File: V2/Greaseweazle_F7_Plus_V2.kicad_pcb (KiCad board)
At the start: 2 copper layers, 80 x 50 mm, 73 parts, among them J1 Wurth 694106301002, J10 PIN1X2, J11 PIN1X2, J12 IDC Box Header, J2 USB_B, J3 Molex 105017-1001, J4 TE EI 171826-4, J5 PIN1X3, J6 PIN1X2, J7 PIN1X5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

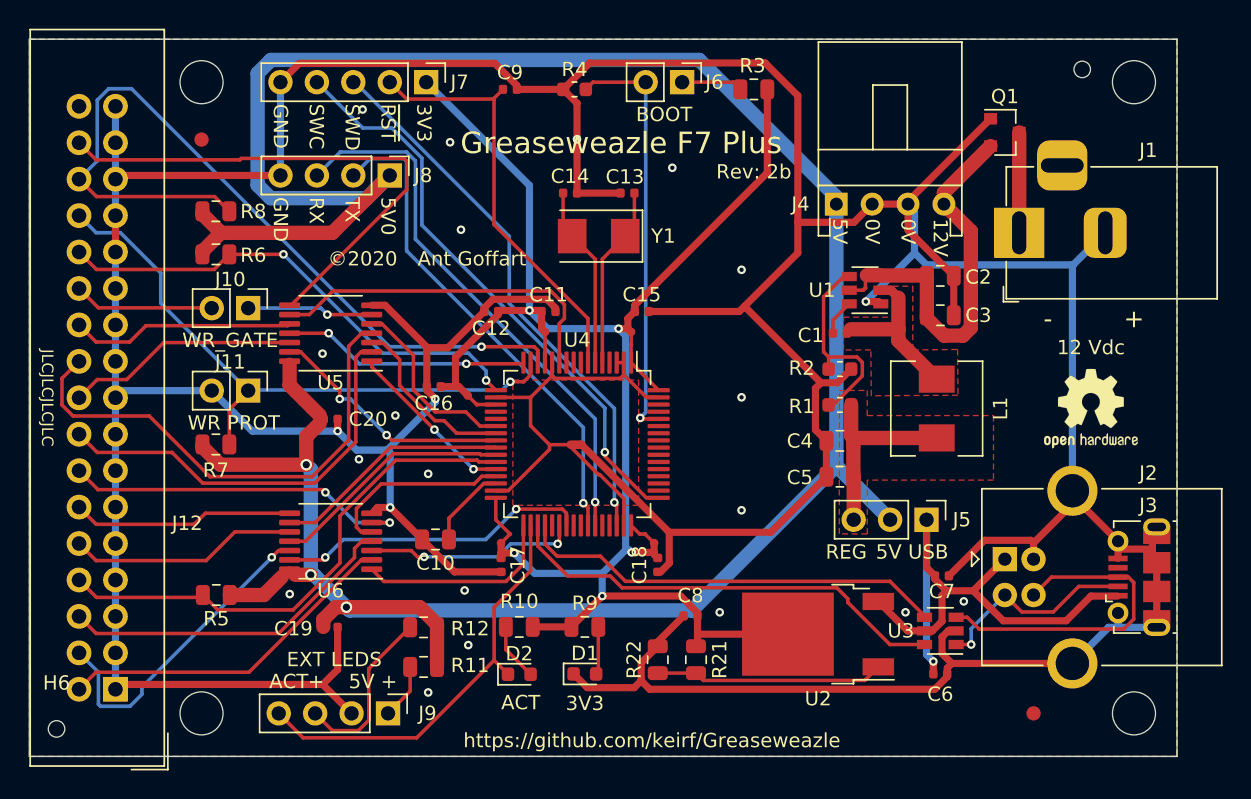
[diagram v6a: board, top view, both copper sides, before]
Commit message: added 3x 10000uF caps to buffer motor start of floppy which can draw up to 1A
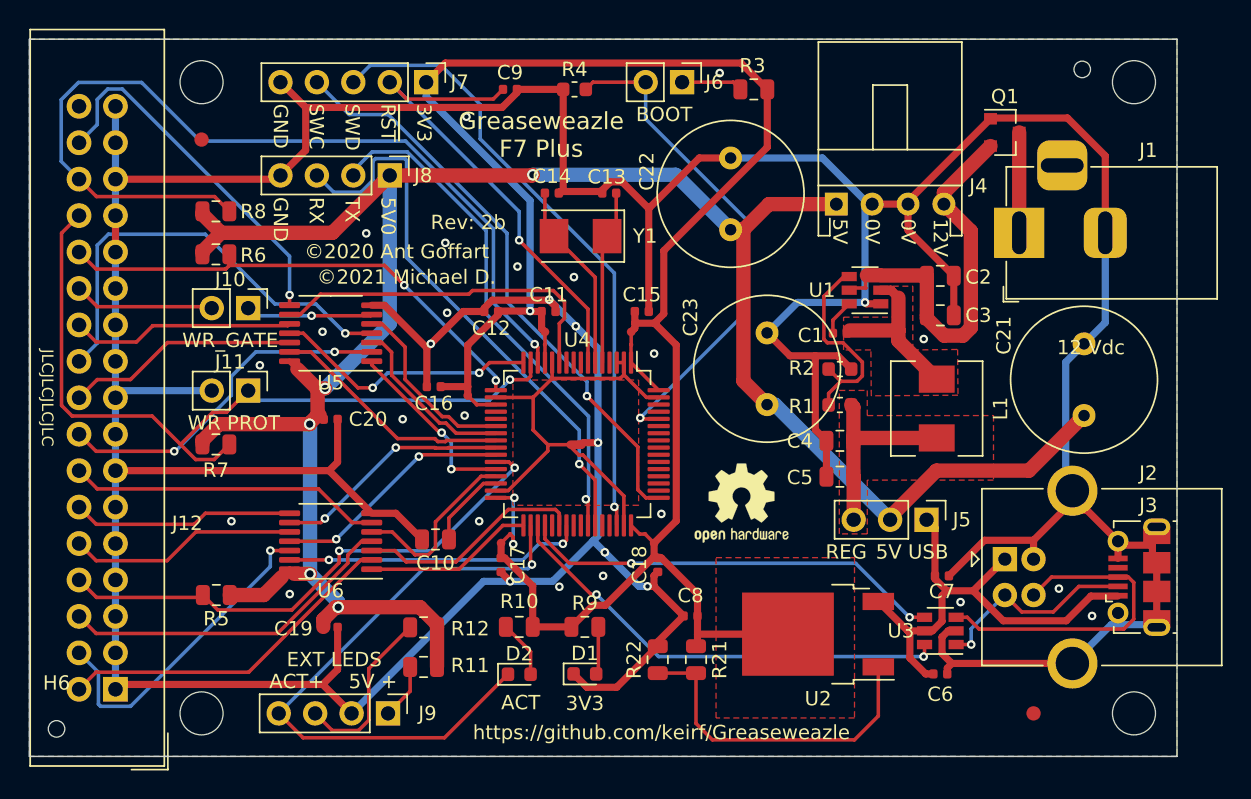
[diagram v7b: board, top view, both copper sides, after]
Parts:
- added C21: 1000uF, Capacitor_THT:C_Radial_D10.0mm_H20.0mm_P5.00mm, F.Cu at (223.5, 126.2)
- added C22: 1000uF, Capacitor_THT:C_Radial_D10.0mm_H20.0mm_P5.00mm, F.Cu at (198.9, 113.3)
- added C23: 1000uF, Capacitor_THT:C_Radial_D10.0mm_H20.0mm_P5.00mm, F.Cu at (201.4, 125.5)
- moved LOGO1 25.2 mm to (199.6, 132.3)
- moved C13 1.27 mm to (190.4, 110.7)
- moved C14 1.27 mm to (186.4, 110.7)
- moved Y1 1.27 mm to (188.4, 113.7)
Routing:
- net +5V: track 189.4 -> 156.2 mm, vias 3 -> 5
- net +3V3: track 113.5 -> 128.7 mm, vias 5 -> 1
- net GND: track 403.6 -> 389.5 mm, vias 23 -> 30
- net /ACT: track 29.8 -> 43.2 mm, vias 0 -> 1
- net /~WR_PROT~: track 43.4 -> 55.3 mm
- net /~SIDE_5V~: track 37.0 -> 25.5 mm, vias 0 -> 1
- net Net-(R21-Pad2): track 16.0 -> 23.5 mm
- net /USB_VBUS: track 41.0 -> 34.0 mm, vias 1 -> 0
- net /~RD_DAT~: track 56.9 -> 62.9 mm
- net /BOOT: track 29.3 -> 35.1 mm
- net /SWDIO: track 38.6 -> 43.7 mm
- net /~M1_5V~: track 29.1 -> 24.5 mm, vias 0 -> 2
- net /~STEP_5V~: track 35.2 -> 30.9 mm, vias 0 -> 1
- net /~RST~: track 29.8 -> 33.9 mm, vias 0 -> 1
- net /~DS0_5V~: track 24.4 -> 21.9 mm, vias 2 -> 0
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- added copper zone on F.Cu, net +3V3
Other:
- board text added: "©2020 Ant Goffart"
- board text added: "©2021 Michael D."
- board text removed: "-"
- board text removed: "Ant Goffart"
- board text removed: "©2020"

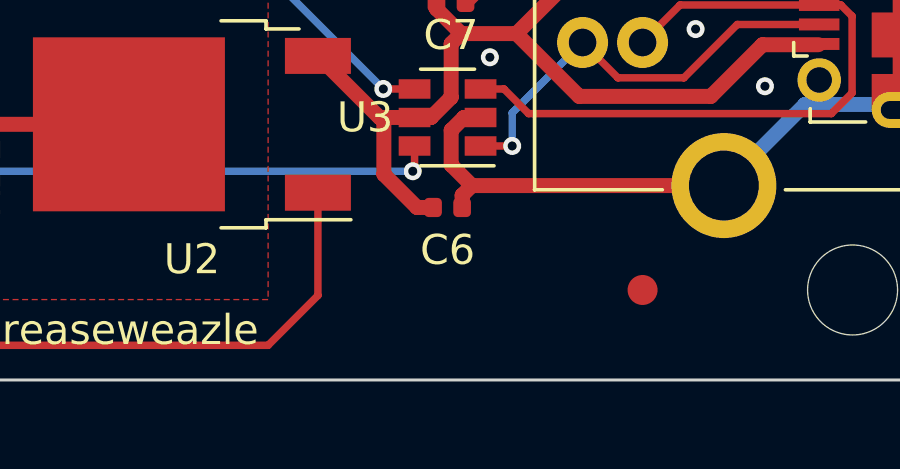
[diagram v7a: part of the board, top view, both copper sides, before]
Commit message: fixed copyright and greaseweazel silk
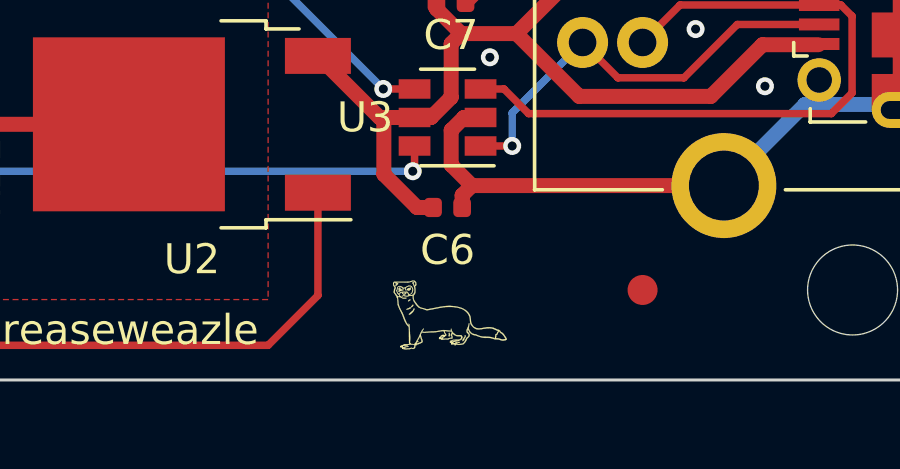
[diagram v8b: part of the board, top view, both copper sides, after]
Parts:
- added LOGO2: Greaseweazle Logo, greaseweazle:Greaseweazle_Logo_verysmall, F.Cu at (213.6, 147.8)
